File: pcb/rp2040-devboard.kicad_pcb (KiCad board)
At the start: 2 copper layers, 0 parts

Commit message: wip pcb placement
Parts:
- added C301: 1u, Capacitor_SMD:C_1210_3225Metric_Pad1.33x2.70mm_HandSolder, F.Cu at (98.0, 99.3)
- added C302: 1u, Capacitor_SMD:C_1210_3225Metric_Pad1.33x2.70mm_HandSolder, F.Cu at (98.0, 103.6)
- added C401: TBD, Capacitor_SMD:C_1210_3225Metric_Pad1.33x2.70mm_HandSolder, F.Cu at (98.0, 53.5)
- added C402: 100n, Capacitor_SMD:C_1210_3225Metric_Pad1.33x2.70mm_HandSolder, F.Cu at (98.0, 57.8)
- added C403: 100n, Capacitor_SMD:C_1210_3225Metric_Pad1.33x2.70mm_HandSolder, F.Cu at (98.0, 62.0)
- added C404: 1u, Capacitor_SMD:C_1210_3225Metric_Pad1.33x2.70mm_HandSolder, F.Cu at (98.0, 66.3)
- added C405: 100n, Capacitor_SMD:C_1210_3225Metric_Pad1.33x2.70mm_HandSolder, F.Cu at (98.0, 70.5)
- added C406: 100n, Capacitor_SMD:C_1210_3225Metric_Pad1.33x2.70mm_HandSolder, F.Cu at (104.0, 53.5)
- added C407: 100n, Capacitor_SMD:C_1210_3225Metric_Pad1.33x2.70mm_HandSolder, F.Cu at (104.0, 57.8)
- added C408: 100n, Capacitor_SMD:C_1210_3225Metric_Pad1.33x2.70mm_HandSolder, F.Cu at (104.0, 62.0)
- added C409: 100n, Capacitor_SMD:C_1210_3225Metric_Pad1.33x2.70mm_HandSolder, F.Cu at (104.0, 66.3)
- added C410: 100n, Capacitor_SMD:C_1210_3225Metric_Pad1.33x2.70mm_HandSolder, F.Cu at (104.0, 70.5)
- added C411: 100n, Capacitor_SMD:C_1210_3225Metric_Pad1.33x2.70mm_HandSolder, F.Cu at (110.0, 53.5)
- added C412: 1u, Capacitor_SMD:C_1210_3225Metric_Pad1.33x2.70mm_HandSolder, F.Cu at (110.0, 57.8)
- added C413: 15p, Capacitor_SMD:C_1210_3225Metric_Pad1.33x2.70mm_HandSolder, F.Cu at (110.0, 62.0)
- added C414: 15p, Capacitor_SMD:C_1210_3225Metric_Pad1.33x2.70mm_HandSolder, F.Cu at (110.0, 66.3)
- added C501: 100n, Capacitor_SMD:C_1210_3225Metric_Pad1.33x2.70mm_HandSolder, F.Cu at (128.0, 91.3)
- added D201: ESD441, rp2040-devboard:Texas_X2SON-DPL-2, F.Cu at (111.2, 91.4)
- added D202: ESD321, Diode_SMD:D_SOD-523, F.Cu at (108.5, 91.5)
- added D203: ESD321, Diode_SMD:D_SOD-523, F.Cu at (108.5, 94.0)
- added J201: USB_C_Receptacle_USB2.0_16P, Connector_USB:USB_C_Receptacle_GCT_USB4105-xx-A_16P_TopMnt_Horizontal, F.Cu at (156.0, 51.5)
- added J601: Conn_01x20, Connector_PinHeader_2.54mm:PinHeader_1x20_P2.54mm_Vertical, F.Cu at (141.5, 55.3)
- added J602: Conn_01x20, Connector_PinHeader_2.54mm:PinHeader_1x20_P2.54mm_Vertical, F.Cu at (170.8, 55.2)
- added J603: Conn_01x03, Connector_PinHeader_2.54mm:PinHeader_1x03_P2.54mm_Vertical, F.Cu at (153.7, 105.8)
- added R201: 5.1k 10%, Resistor_SMD:R_1210_3225Metric_Pad1.30x2.65mm_HandSolder, F.Cu at (109.7, 84.0)
- added R202: 5.1k 10%, Resistor_SMD:R_1210_3225Metric_Pad1.30x2.65mm_HandSolder, F.Cu at (109.7, 88.2)
- added R401: TBD, Resistor_SMD:R_1210_3225Metric_Pad1.30x2.65mm_HandSolder, F.Cu at (157.0, 86.2)
- added R402: 27R, Resistor_SMD:R_1210_3225Metric_Pad1.30x2.65mm_HandSolder, F.Cu at (116.0, 57.7)
- added R403: 27R, Resistor_SMD:R_1210_3225Metric_Pad1.30x2.65mm_HandSolder, F.Cu at (116.0, 61.9)
- added R501: TBD, Resistor_SMD:R_1210_3225Metric_Pad1.30x2.65mm_HandSolder, F.Cu at (128.0, 95.5)
- added SW401: SW_Push, rp2040-devboard:SW_SPST_EVPBV, F.Cu at (93.4, 83.5)
- added SW501: SW_Push, rp2040-devboard:SW_SPST_EVPBV, F.Cu at (162.2, 63.9)
- added U301: TC1017-xLT, Package_TO_SOT_SMD:SOT-353_SC-70-5, F.Cu at (103.1, 99.2)
- added U401: RP2040, Package_DFN_QFN:QFN-56-1EP_7x7mm_P0.4mm_EP3.2x3.2mm, F.Cu at (155.3, 74.6)
- added U501: W25Q128JVS, Package_SO:SOIC-8_5.23x5.23mm_P1.27mm, F.Cu at (150.9, 62.4)
- added Y401: ABM8-272-T3, Crystal:Crystal_SMD_3225-4Pin_3.2x2.5mm, F.Cu at (150.7, 86.1)
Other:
- board outline added: 34 x 59 mm

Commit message: wip pcb placement
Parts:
- removed the R401 at (157.0, 86.2)
- moved C301 80.7 mm to (167.3, 58.0)
- moved C302 80.0 mm to (168.1, 65.0)
- moved C401 76.9 mm to (166.2, 89.0), turned to 180 degrees
- moved SW401 74.6 mm to (166.8, 96.9), turned to 90 degrees
- moved U301 74.0 mm to (166.9, 61.6), turned to -90 degrees
- moved C402 71.6 mm to (165.7, 81.0)
- moved C403 71.3 mm to (165.7, 84.2)
- moved R202 68.7 mm to (166.8, 50.0)
- moved C408 64.8 mm to (167.2, 76.2)
- moved C409 63.6 mm to (167.2, 72.8)
- moved D201 62.3 mm to (163.0, 56.8), turned to 90 degrees
- moved C407 62.3 mm to (160.8, 83.5), turned to -90 degrees
- moved D202 61.0 mm to (160.2, 59.2)
- moved C412 59.6 mm to (168.5, 69.0)
- moved D203 59.1 mm to (156.2, 59.2), turned to 180 degrees
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- renumbered R402 to R401, R403 to R402
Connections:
- J602 pad 4: /IO/GPIO26_ADC0 -> /IO/GPIO29_ADC3
- J602 pad 5: /IO/GPIO27_ADC1 -> /IO/GPIO28_ADC2
- J602 pad 6: /IO/GPIO28_ADC2 -> /IO/GPIO27_ADC1
- J602 pad 7: /IO/GPIO29_ADC3 -> /IO/GPIO26_ADC0
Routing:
- added copper zone on B.Cu, net GND
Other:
- board size 34 x 59 mm -> 37.8 x 62.5 mm

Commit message: change footprint
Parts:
- C301, C302, C401, C402, C403, C404, C405, C406, C407, C408, C409, C410, C411, C412, C413, C414, C501: footprint Capacitor_SMD:C_1210_3225Metric_Pad1.33x2.70mm_HandSolder -> Capacitor_SMD:C_0603_1608Metric_Pad1.08x0.95mm_HandSolder
- R201, R202, R401, R402, R501: footprint Resistor_SMD:R_1210_3225Metric_Pad1.30x2.65mm_HandSolder -> Resistor_SMD:R_0603_1608Metric_Pad0.98x0.95mm_HandSolder
- moved C404 15.6 mm to (133.9, 70.8)

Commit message: wip pcb placement
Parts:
- removed the D201 at (163.0, 56.8)
- added C201: 1u, Capacitor_SMD:C_0603_1608Metric_Pad1.08x0.95mm_HandSolder, F.Cu at (168.9, 51.5)
- added C202: 1u, Capacitor_SMD:C_0603_1608Metric_Pad1.08x0.95mm_HandSolder, F.Cu at (166.8, 57.0)
- added U201: NCP360SN, Package_SO:TSOP-5_1.65x3.05mm_P0.95mm, F.Cu at (166.8, 54.2)
- moved C410 35.2 mm to (159.0, 83.8), turned to -90 degrees
- moved C404 28.4 mm to (162.2, 68.7), turned to 90 degrees
- moved C501 25.5 mm to (148.8, 59.0), turned to 90 degrees
- moved C411 24.4 mm to (147.9, 77.0), turned to 180 degrees
- moved C402 18.6 mm to (155.8, 65.2), turned to 90 degrees
- moved C407 15.4 mm to (165.2, 68.7), turned to 90 degrees
- moved C405 8.72 mm to (157.2, 65.2), turned to 90 degrees
- moved R501 8.28 mm to (155.5, 90.2), turned to 180 degrees
- moved R202 8.14 mm to (161.2, 56.0)
- moved R201 7.96 mm to (154.8, 56.0)
- moved C409 5.27 mm to (166.8, 78.0)
- moved C403 5.21 mm to (160.5, 83.8), turned to -90 degrees
- moved C412 4.76 mm to (163.8, 68.7), turned to 90 degrees
- moved C408 4.32 mm to (166.5, 72.0)
- moved R401 4.27 mm to (159.0, 68.0)
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- renumbered D202 to D201, D203 to D202
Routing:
- net +3V3: track 0.00 -> 73.1 mm, vias 0 -> 2
- net GND: track 0.00 -> 52.4 mm, vias 0 -> 45
- net /Flash/QSPI_SS: track 0.00 -> 42.0 mm, vias 0 -> 2
- net /IO/GPIO15: track 0.00 -> 31.7 mm
- net +1V1: track 0.00 -> 31.1 mm, vias 0 -> 3
- net /IO/GPIO16: track 0.00 -> 29.8 mm
- net /IO/SWCLK: track 0.00 -> 29.1 mm
- net /IO/GPIO14: track 0.00 -> 29.1 mm
- net /IO/SWD: track 0.00 -> 27.5 mm
- net /IO/GPIO17: track 0.00 -> 27.4 mm
- net /IO/GPIO0: track 0.00 -> 27.4 mm
- net /IO/GPIO1: track 0.00 -> 25.3 mm
- net /IO/GPIO13: track 0.00 -> 24.0 mm
- net /IO/GPIO18: track 0.00 -> 21.9 mm
- net /IO/GPIO12: track 0.00 -> 21.2 mm
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- added copper zone on F.Cu, net +3V3
- added copper zone on F.Cu, net +5V
- added copper zone on F.Cu, net VBUS
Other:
- board size 37.8 x 62.5 mm -> 37.8 x 60.5 mm
- board text added: "3V3"
- board text added: "5V"
- board text added: "BOOTSEL"
- board text added: "GND"
- board text added: "GPIO0"
- board text added: "GPIO1"
- board text added: "GPIO10"
- board text added: "GPIO11"
- board text added: "GPIO12"
- board text added: "GPIO13"
- board text added: "GPIO14"
- board text added: "GPIO15"
- board text added: "GPIO16"
- board text added: "GPIO17"
- board text added: "GPIO18"
- board text added: "GPIO19"
- board text added: "GPIO2"
- board text added: "GPIO20"
- board text added: "GPIO21"
- board text added: "GPIO22"
- board text added: "GPIO23"
- board text added: "GPIO24"
- board text added: "GPIO25"
- board text added: "GPIO26"
- board text added: "GPIO27"
- board text added: "GPIO28"
- board text added: "GPIO29"
- board text added: "GPIO3"
- board text added: "GPIO4"
- board text added: "GPIO5"
- board text added: "GPIO6"
- board text added: "GPIO7"
- board text added: "GPIO8"
- board text added: "GPIO9"
- board text added: "RESET"
- board text added: "RP2040"
- board text added: "SWCLK"
- board text added: "SWD"
- board text added: "rp2040-devboard"

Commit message: finish routing
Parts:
- moved D202 2.47 mm to (158.5, 60.0)
- moved C301 1.25 mm to (164.0, 60.8)
- moved C302 1.25 mm to (168.5, 63.2)
- moved U301 1.25 mm to (166.8, 60.8)
- moved D201 1.08 mm to (161.0, 58.2)
- moved R201 0.75 mm to (154.0, 56.0)
- moved R202 0.75 mm to (162.0, 56.0)
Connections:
- net Net-(U401-USB_DM) renamed /rp2040/USB_TERM_D-
- net Net-(U401-USB_DP) renamed /rp2040/USB_TERM_D+
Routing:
- net +3V3: track 73.1 -> 74.1 mm
- net Net-(J201-CC1): track 2.52 -> 3.05 mm

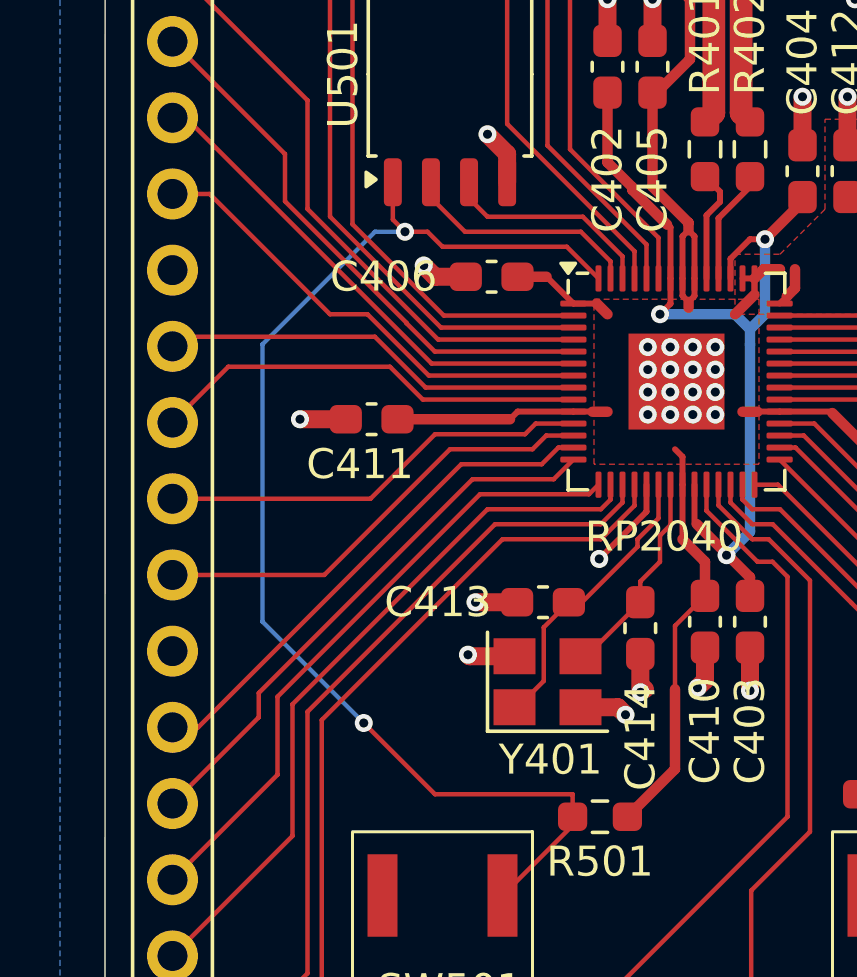
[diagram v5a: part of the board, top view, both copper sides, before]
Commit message: mirror back silkscreen
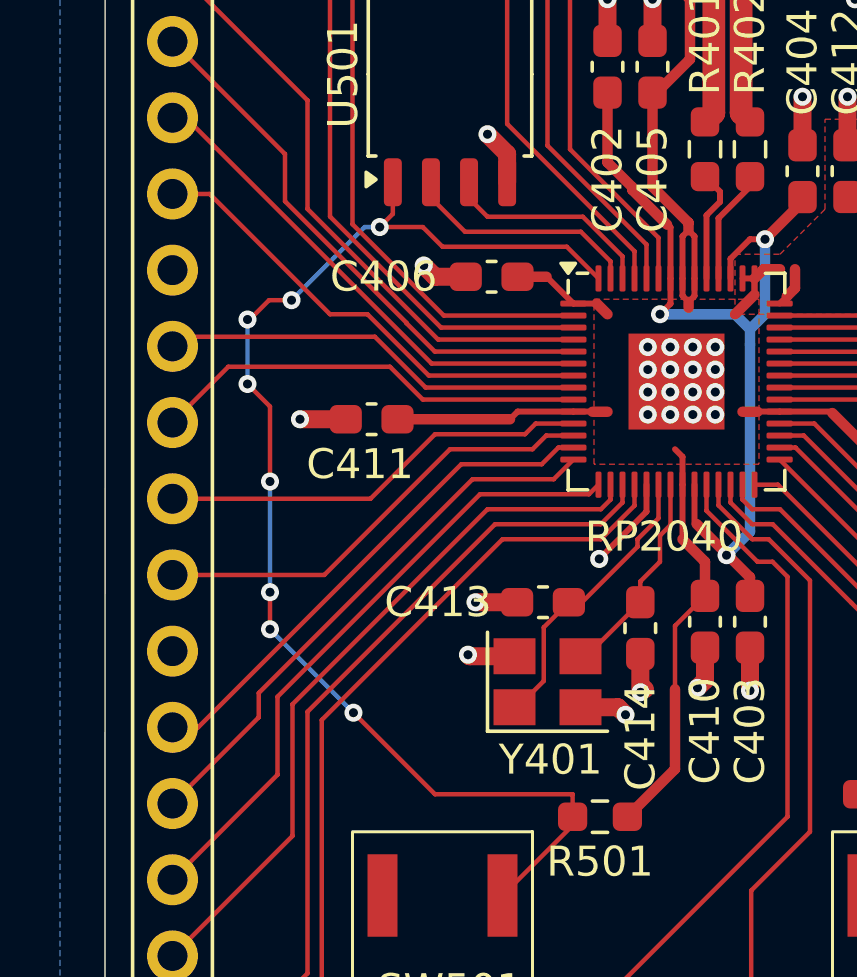
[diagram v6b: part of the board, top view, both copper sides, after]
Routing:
- net /Flash/QSPI_SS: track 42.0 -> 43.2 mm, vias 2 -> 8

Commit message: add debouncing capacitor value and dnp pull up
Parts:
- C401: value TBD -> 1u
- R501: value TBD -> DNF
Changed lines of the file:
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@@
 			)
 		)
+		(property "Distributor link" "https://mou.sr/3yOwNm4"
+			(at 0 0 0)
+			(unlocked yes)
+			(layer "F.Fab")
+			(hide yes)
+			(effects
+				(font
+					(size 1 1)
+					(thickness 0.15)
+				)
+			)
+		)
 		(property ki_fp_filters "QFN*1EP*7x7mm?P0.4mm*")
 		(sheetname "rp2040")
@@
 			)
 		)
-		(property "Value" "TBD"
+		(property "Value" "1u"
 			(at 0 1.43 180)
 			(layer "F.Fab")
@@
 			)
 		)
-		(property "Value" "TBD"
+		(property "Value" "DNF"
 			(at 0 1.43 0)
 			(layer "F.Fab")
@@
 		(sheetname "Flash")
 		(sheetfile "flash.kicad_sch")
-		(attr smd)
+		(attr smd dnp)
 		(fp_line
 			(start -0.254724 0.5225)
